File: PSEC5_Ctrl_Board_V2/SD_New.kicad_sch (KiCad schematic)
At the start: 15 parts, among them IC2 NVT4858HKZ, J8 1040310811, U22 TPS22913BYZVT, U23 NX3P1108UKZ, U25 NX3P1108UKZ

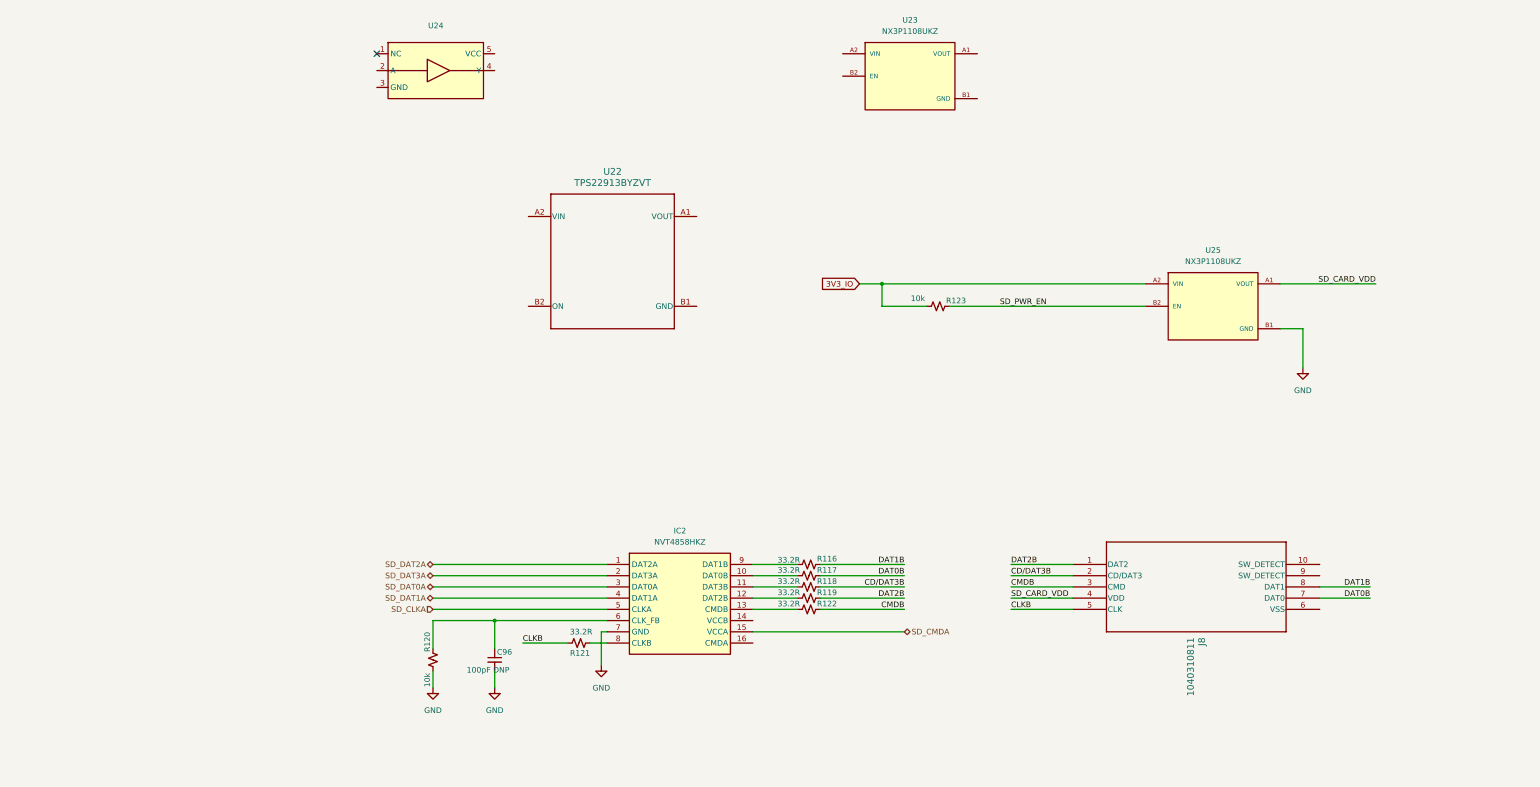
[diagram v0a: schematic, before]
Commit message: Updated Schematic with New SD implemented
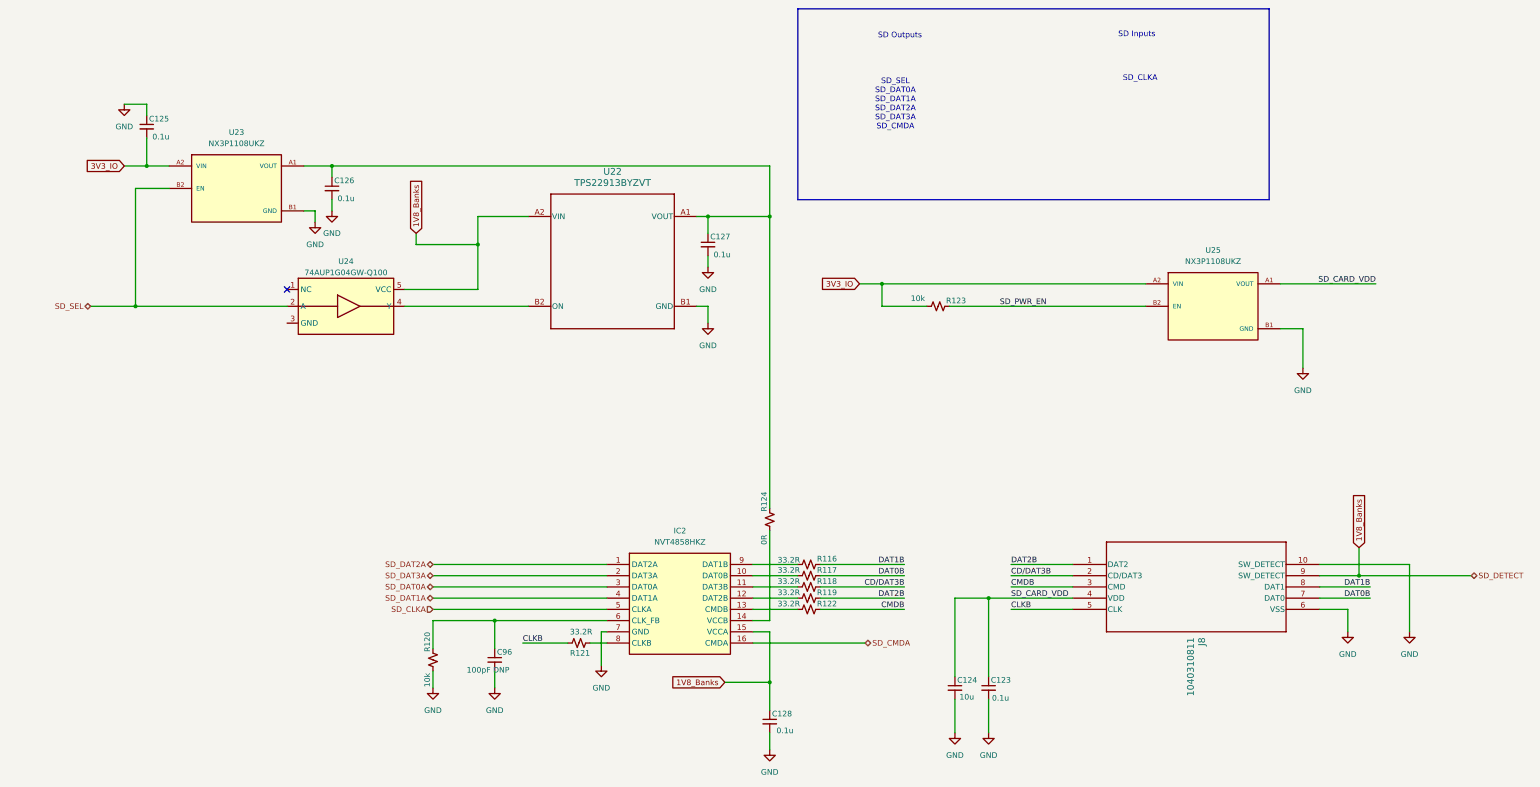
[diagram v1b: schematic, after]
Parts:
- added C123, C125, C126, C127, C128: 0.1u, Capacitor_SMD:C_0603_1608Metric, symbol Device:C_Small
- added C124: 10u, Capacitor_SMD:C_0603_1608Metric, symbol Device:C_Small
- added R124: 0R, Resistor_SMD:R_0603_1608Metric, symbol Device:R_Small_US
- U24: value ~ -> 74AUP1G04GW-Q100
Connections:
- net 3V3_IO: now also U23.A2 (VIN), C125.2
- net GND: now also J8.10 (SW_DETECT), J8.6 (VSS), U22.B1 (GND), U23.B1 (GND), C123.2, C124.2, C125.1, C126.2, C127.2, C128.2
- net SD_CARD_VDD: now also C123.1, C124.1
- net SD_CMDA: now also IC2.16 (CMDA); no longer IC2.15 (VCCA)
- net SD_SEL: now reaches U24.2 (A)
- net SD_SEL: now also U23.B2 (EN)
- net at U24.4 (Y): now also U22.B2 (ON)
- net 1V8_Banks: now reaches U24.5 (VCC)
- net 1V8_Banks: now also IC2.15 (VCCA), J8.9 (SW_DETECT), U22.A2 (VIN), C128.1
- net at U22.A1 (VOUT): now also U23.A1 (VOUT), C126.1, C127.1, R124.2
- net at IC2.14 (VCCB): now also R124.1
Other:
- note added: "SD Inputs"
- note added: "SD Outputs"
- note added: "SD_CLKA"
- note added: "SD_SEL SD_DAT0A SD_DAT1A SD_DAT2A SD_DAT3A SD_CMDA"
- moved on the sheet: U23, U24

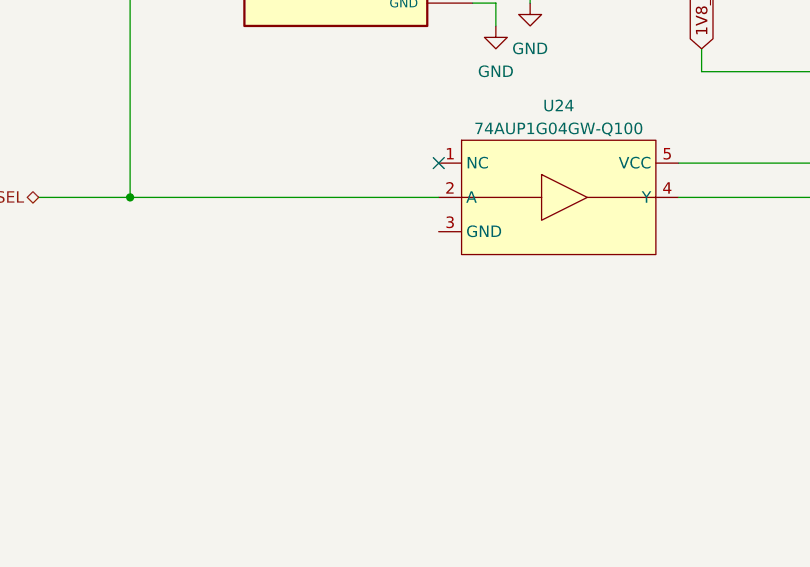
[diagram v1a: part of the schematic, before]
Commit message: fixed small ERC errors
Added no connection on open pins
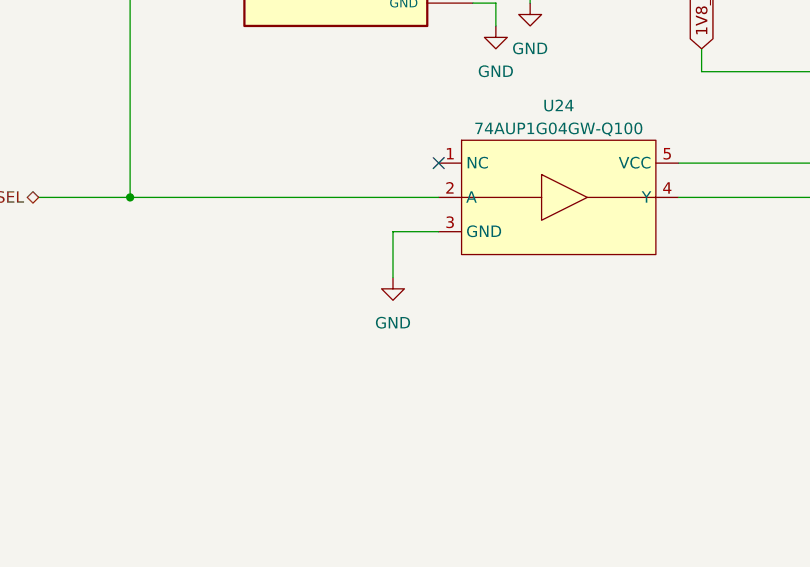
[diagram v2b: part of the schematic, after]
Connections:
- net GND: now also U24.3 (GND)
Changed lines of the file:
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@@
+	(wire
+		(pts
+			(xy 67.31 86.36) (xy 67.31 91.44)
+		)
+		(stroke
+			(width 0)
+			(type default)
+		)
+	)
 	(wire
 		(pts
@@
 		(pts
 			(xy 201.93 77.47) (xy 207.01 77.47)
+		)
+		(stroke
+			(width 0)
+			(type default)
+		)
+	)
+	(wire
+		(pts
+			(xy 72.39 86.36) (xy 67.31 86.36)
 		)
 		(stroke
@@
 					(unit 1)
 				)
+			)
+		)
+	)
+	(symbol
+		(lib_id "power:GND")
+		(at 67.31 91.44 0)
+		(unit 1)
+		(exclude_from_sim no)
+		(in_bom yes)
+		(on_board yes)
+		(dnp no)
+		(fields_autoplaced yes)
+		(property "Reference" "#PWR048"
+			(at 67.31 97.79 0)
+			(effects
+				(font
+					(size 1.27 1.27)
+				)
+				(hide yes)
+			)
+		)
+		(property "Value" "GND"
+			(at 67.31 96.52 0)
+			(effects
+				(font
+					(size 1.27 1.27)
+				)
+			)
+		)
+		(property "Footprint" ""
+			(at 67.31 91.44 0)
+			(effects
+				(font
+					(size 1.27 1.27)
+				)
+				(hide yes)
+			)
+		)
+		(property "Datasheet" ""
+			(at 67.31 91.44 0)
+			(effects
+				(font
+					(size 1.27 1.27)
+				)
+				(hide yes)
+			)
+		)
+		(property "Description" "Power symbol creates a global label with name \"GND\" , ground"
+			(at 67.31 91.44 0)
+			(effects
+				(font
+					(size 1.27 1.27)
+				)
+				(hide yes)
+			)
+		)
+		(pin "1"
+		)
+		(instances
+			(project ""
+				(path "/165f2ae6-d522-4adf-a6c4-bb137b209d33/1f6d7a03-cfad-4370-8d2b-49ab19e248d8/15f57d5c-54b3-4ba8-a361-8040b738c0f2"
+					(reference "#PWR048")
+					(unit 1)
+				)

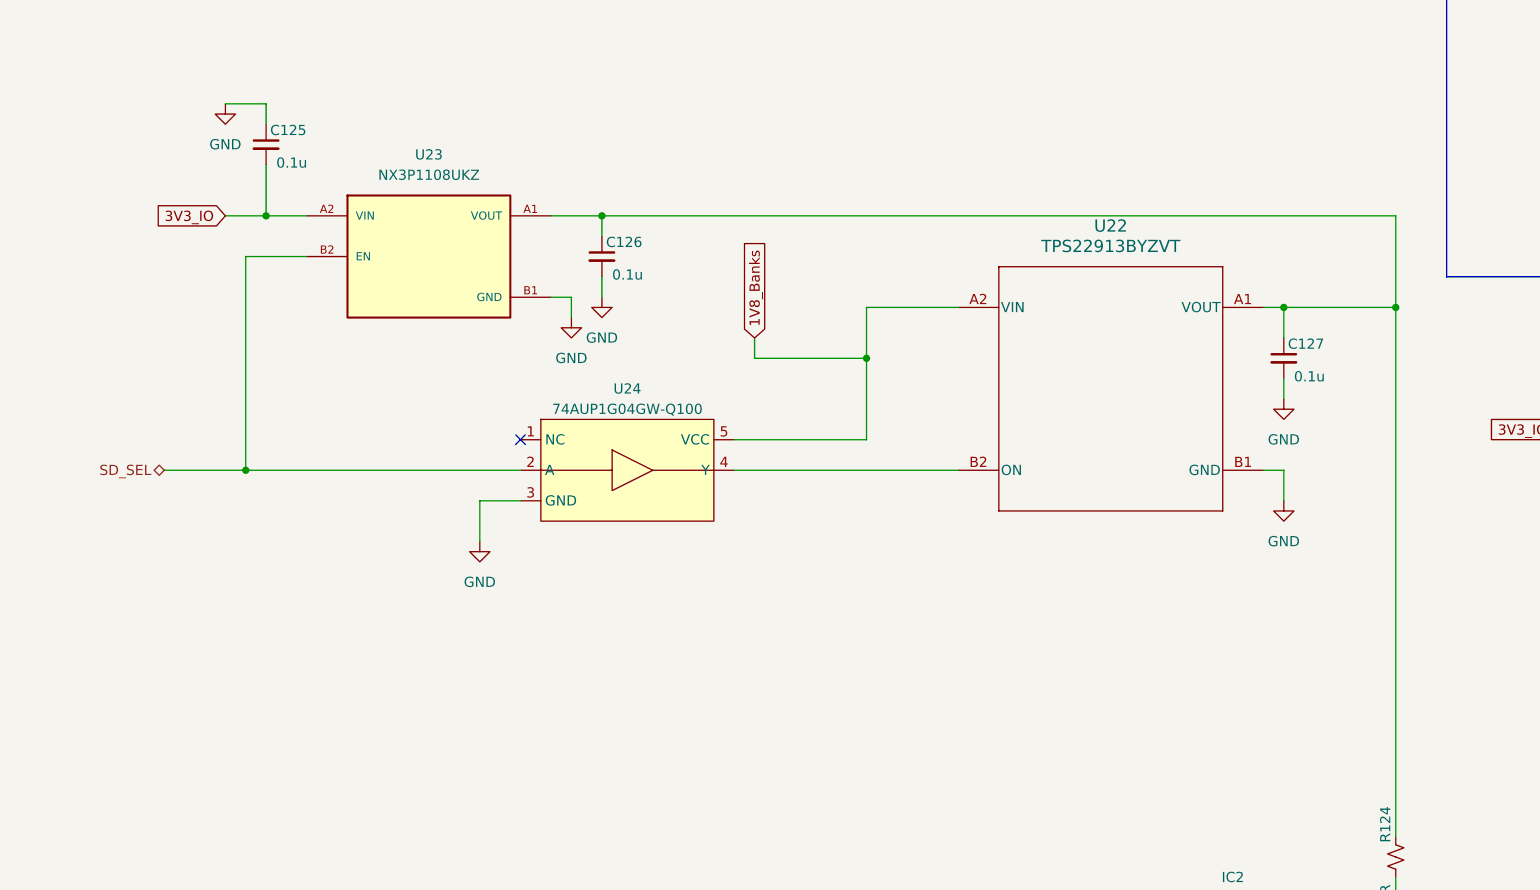
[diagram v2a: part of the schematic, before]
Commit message: Updated Joes Initial Comments. Schematic should be functional
Fixed Joes comments. Still discrepancy on the inversion signal during Voltage Handshake. However, added inverter signal that we can turn on or off depending on what is desired.
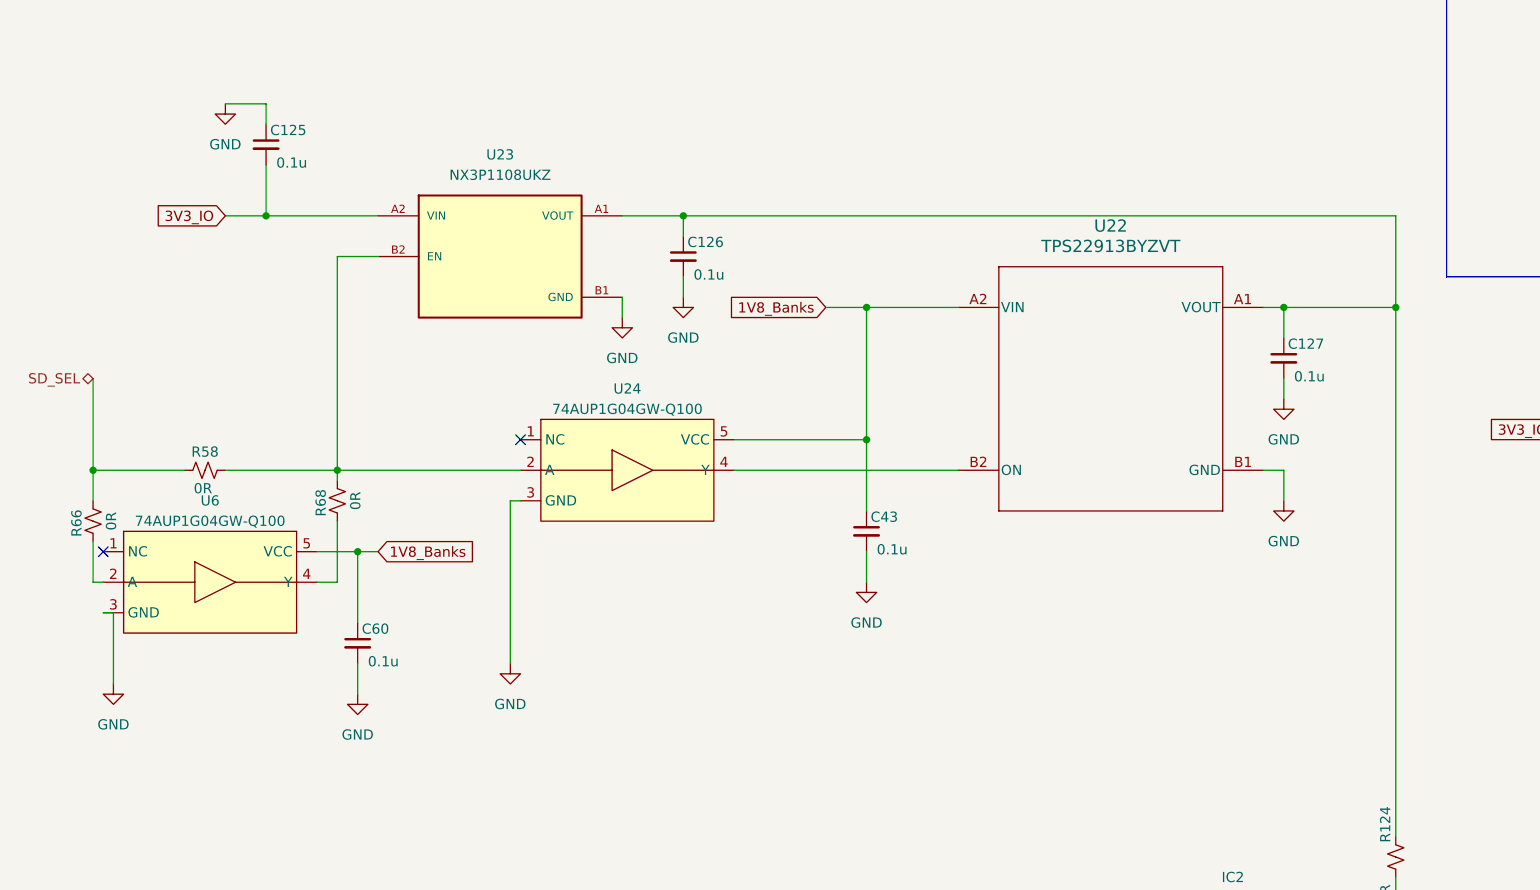
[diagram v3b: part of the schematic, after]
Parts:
- added C43, C60: 0.1u, Capacitor_SMD:C_0603_1608Metric, symbol Device:C_Small
- added R58, R66, R68: 0R, Resistor_SMD:R_0603_1608Metric, symbol Device:R_Small_US
- added U6: 74AUP1G04GW-Q100, Package_TO_SOT_SMD:SOT-353_SC-70-5, symbol 74AUP1G04GW:74AUP1G04GW-Q100
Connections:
- net 1V8_Banks: now also C43.1, C60.1, U6.5 (VCC)
- net GND: now also C43.2, C60.2, U6.3 (GND)
- net SD_SEL: now also R58.2, R66.1; no longer U23.B2 (EN), U24.2 (A)
- new net: R58.1, R68.1, U23.B2 (EN), U24.2 (A)
- new net: R68.2, U6.4 (Y)
- new net: R66.2, U6.2 (A)
- no-connect marks 1 -> 2
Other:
- moved on the sheet: C126, U23
